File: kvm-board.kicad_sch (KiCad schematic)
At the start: 21 parts, among them J1 TYPE-C-31-M-12, J2 TYPE-C-31-M-12, U1 CH9329, U2 CH340N

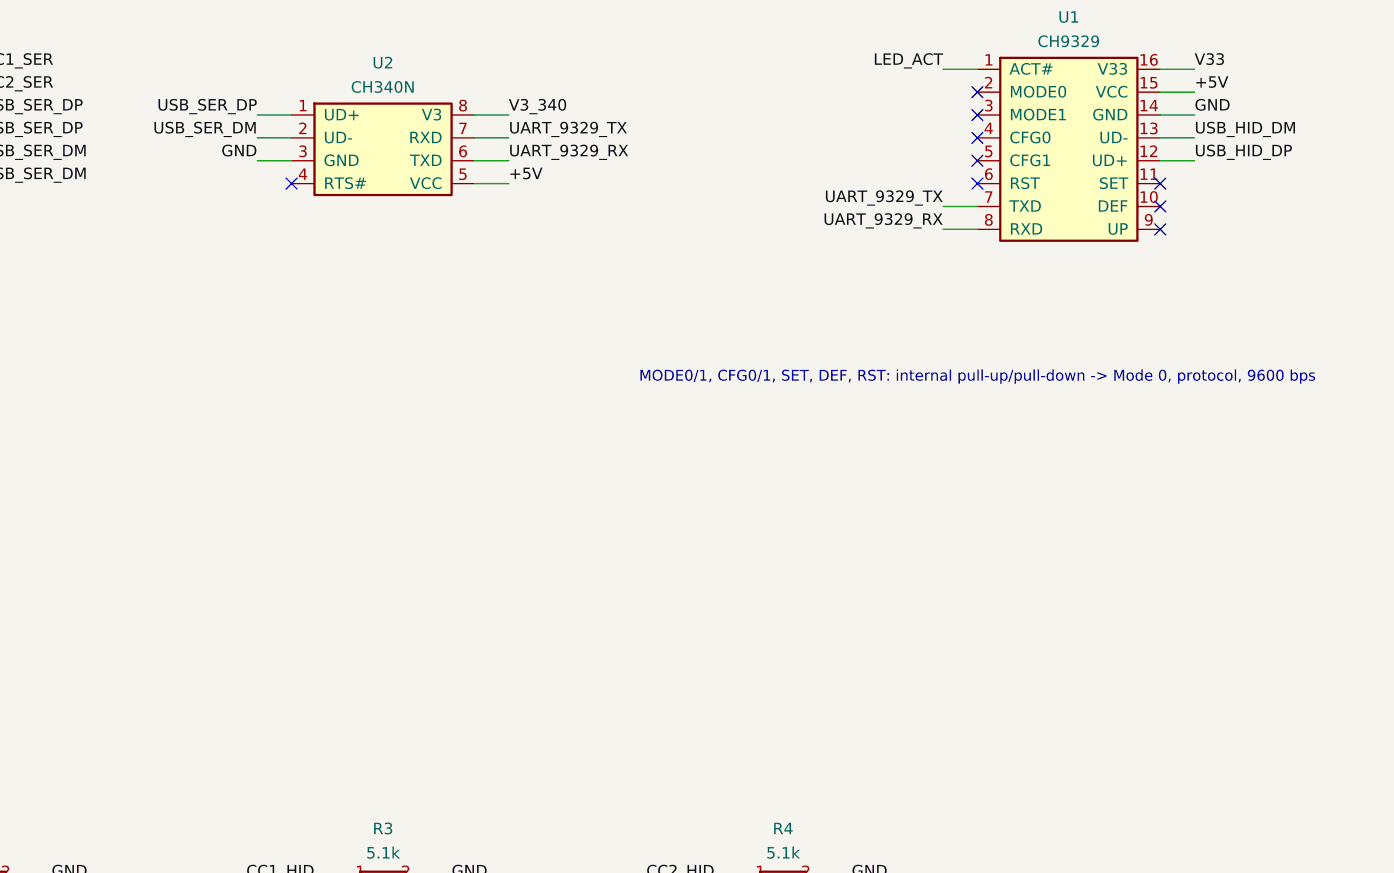
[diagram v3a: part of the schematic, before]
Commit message: Add SET/GND test pads and a repository QR code
TP1/TP2 break out the CH9329 SET pin and GND so the WCH config tool can be used without soldering to U1. Both are bare 1.7 mm pads on 2.54 mm pitch and are excluded from the BOM and CPL.

The bottom silkscreen now carries a QR code for https://github.com/nananek/kvm-board. The matrix is checked in as scripts/repo_qr.txt; scripts/make_repo_qr.py regenerates it when the URL changes.
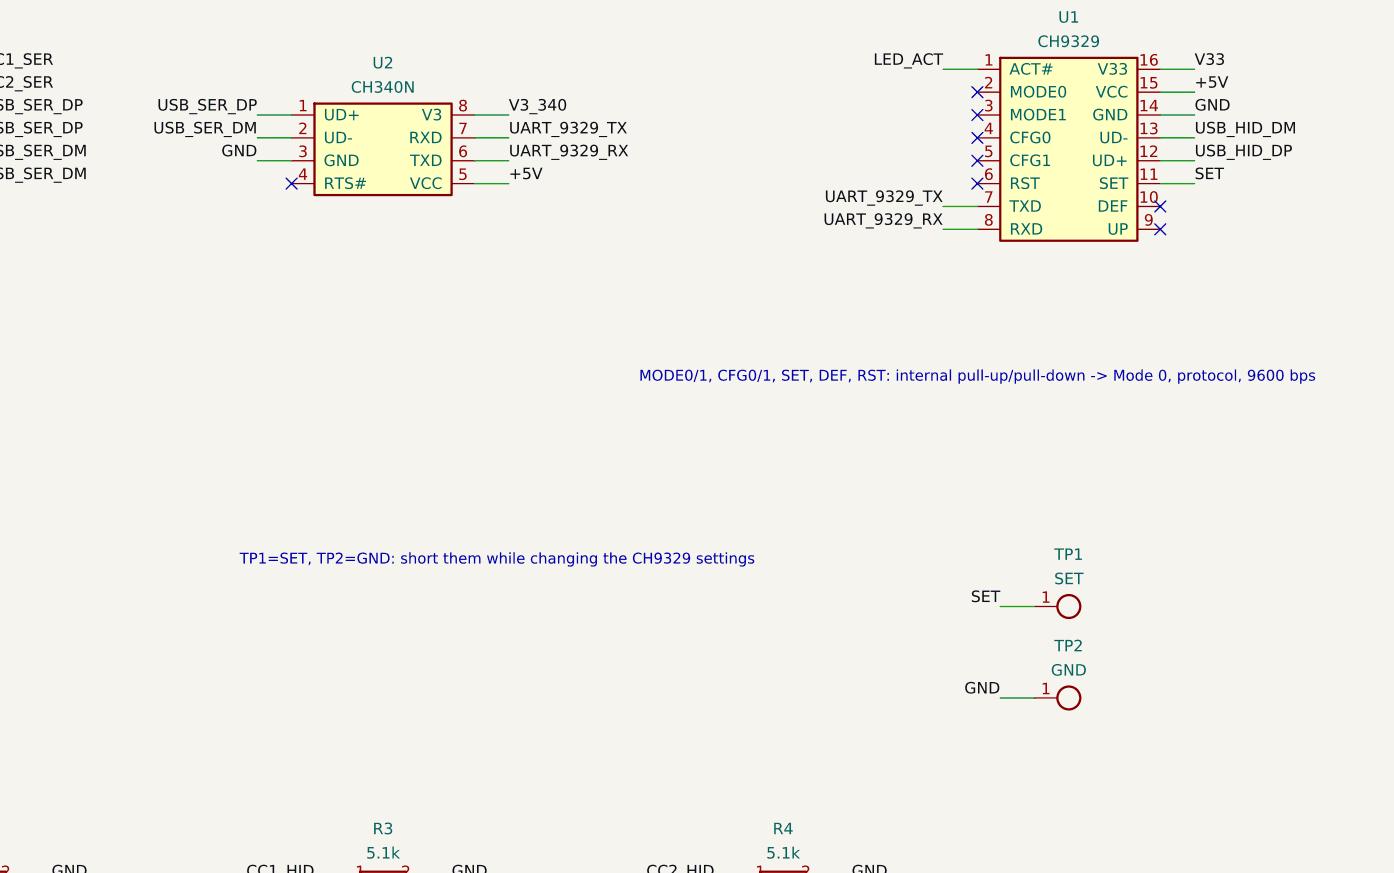
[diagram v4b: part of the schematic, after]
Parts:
- added TP1: SET, KVM:TestPoint_1P, symbol kvm:TP
- added TP2: GND, KVM:TestPoint_1P, symbol kvm:TP
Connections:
- net GND: now also TP2.1
- net SET: now reaches U1.11 (SET)
- net SET: now also TP1.1
- no-connect marks 13 -> 12
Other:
- note added: "TP1=SET, TP2=GND: short them while changing the CH9329 settings"
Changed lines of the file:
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@@
   (text "UART: U2.TXD(6) -> U1.RXD(8), U1.TXD(7) -> U2.RXD(7)" (at 177.8 69.85 0) (effects (font (size 1.2 1.2))))
   (text "MODE0/1, CFG0/1, SET, DEF, RST: internal pull-up/pull-down -> Mode 0, protocol, 9600 bps" (at 205.74 114.3 0) (effects (font (size 1.2 1.2))))
+  (text "TP1=SET, TP2=GND: short them while changing the CH9329 settings" (at 152.4 134.62 0) (effects (font (size 1.2 1.2))))
   (symbol (lib_id "kvm:USB_C") (at 76.2 88.9 0) (unit 1)
     (exclude_from_sim no) (in_bom yes) (on_board yes) (dnp no)
@@
   (wire (pts (xy 226.06 90.17) (xy 229.87 90.17)) (stroke (width 0) (type default)))
   (label "USB_HID_DP" (at 229.87 90.17 0) (effects (font (size 1.27 1.27)) (justify left bottom)))
-  (no_connect (at 226.06 92.71))
+  (wire (pts (xy 226.06 92.71) (xy 229.87 92.71)) (stroke (width 0) (type default)))
+  (label "SET" (at 229.87 92.71 0) (effects (font (size 1.27 1.27)) (justify left bottom)))
   (no_connect (at 226.06 95.25))
   (no_connect (at 226.06 97.79))
@@
   (wire (pts (xy 323.85 203.2) (xy 327.66 203.2)) (stroke (width 0) (type default)))
   (label "GND" (at 327.66 203.2 0) (effects (font (size 1.27 1.27)) (justify left bottom)))
+  (symbol (lib_id "kvm:TP") (at 215.9 139.7 0) (unit 1)
+    (exclude_from_sim no) (in_bom yes) (on_board yes) (dnp no)
+    (property "Reference" "TP1" (at 215.9 133.93 0) (effects (font (size 1.27 1.27))))
+    (property "Value" "SET" (at 215.9 136.63 0) (effects (font (size 1.27 1.27))))
+    (property "Footprint" "KVM:TestPoint_1P" (at 215.9 139.7 0) (effects (font (size 1.27 1.27)) hide))
+    (property "Datasheet" "" (at 215.9 139.7 0) (effects (font (size 1.27 1.27)) hide))
+    (property "LCSC" "" (at 215.9 139.7 0) (effects (font (size 1.27 1.27)) hide))
+    (pin "1")
+    (instances (project "kvm-board" (path "/0e6e9d0a-6a7b-4f4e-9d3a-6f3f5c2b1a01" (reference "TP1") (unit 1))))
+  )
+  (wire (pts (xy 212.09 139.7) (xy 208.28 139.7)) (stroke (width 0) (type default)))
+  (label "SET" (at 208.28 139.7 0) (effects (font (size 1.27 1.27)) (justify right bottom)))
+  (symbol (lib_id "kvm:TP") (at 215.9 149.86 0) (unit 1)
+    (exclude_from_sim no) (in_bom yes) (on_board yes) (dnp no)
+    (property "Reference" "TP2" (at 215.9 144.09 0) (effects (font (size 1.27 1.27))))
+    (property "Value" "GND" (at 215.9 146.79 0) (effects (font (size 1.27 1.27))))
+    (property "Footprint" "KVM:TestPoint_1P" (at 215.9 149.86 0) (effects (font (size 1.27 1.27)) hide))
+    (property "Datasheet" "" (at 215.9 149.86 0) (effects (font (size 1.27 1.27)) hide))
+    (property "LCSC" "" (at 215.9 149.86 0) (effects (font (size 1.27 1.27)) hide))
+    (pin "1")
+    (instances (project "kvm-board" (path "/0e6e9d0a-6a7b-4f4e-9d3a-6f3f5c2b1a01" (reference "TP2") (unit 1))))
+  )
+  (wire (pts (xy 212.09 149.86) (xy 208.28 149.86)) (stroke (width 0) (type default)))
+  (label "GND" (at 208.28 149.86 0) (effects (font (size 1.27 1.27)) (justify right bottom)))
   (symbol (lib_id "kvm:PWR_FLAG") (at 152.4 254 0) (unit 1)
     (exclude_from_sim no) (in_bom no) (on_board no) (dnp no)
